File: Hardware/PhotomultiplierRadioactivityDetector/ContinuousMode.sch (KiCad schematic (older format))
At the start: 13 parts, among them U6 TL074

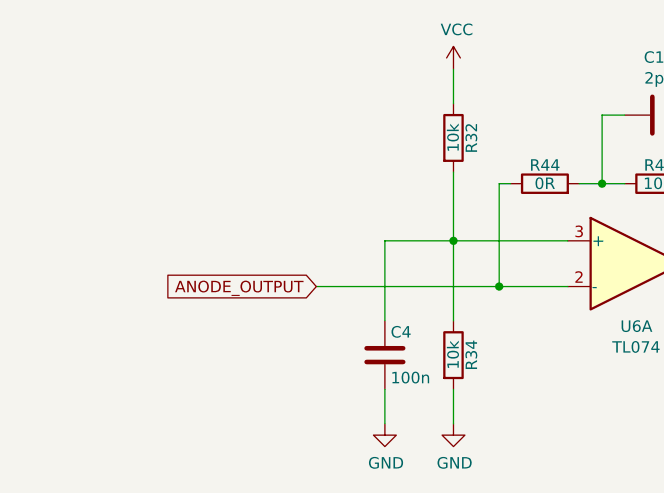
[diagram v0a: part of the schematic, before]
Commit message: add element,, footprint and 3d model for transformer
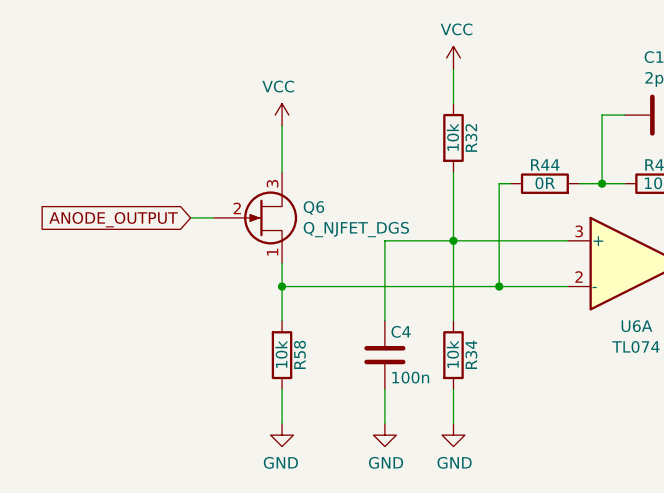
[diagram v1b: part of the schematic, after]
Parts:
- added Q6: Q_NJFET_DGS, Package_TO_SOT_SMD:SC-59, symbol Device:Q_NJFET_DGS
- added R58: 10k, Resistor_SMD:R_0805_2012Metric_Pad1.15x1.40mm_HandSolder, symbol Device:R
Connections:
- net ANODE_OUTPUT: now also Q6.2 (G); no longer R44.1, U6.2 (-)
- net GND: now also R58.1
- net VCC: now also Q6.3 (S)
- new net: Q6.1 (D), R44.1, R58.2, U6.2 (-)
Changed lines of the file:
@@
 $Descr A4 11693 8268
 encoding utf-8
-Sheet 7 7
+Sheet 6 7
 Title ""
 Date ""
@@
 	1    0    0    -1
 $EndComp
-Text GLabel 2600 3450 0    50   Input ~ 0
+Text GLabel 2050 3150 0    50   Input ~ 0
 ANODE_OUTPUT
 Wire Wire Line
 	4350 3350 4850 3350
-Wire Wire Line
-	2600 3450 3400 3450
 Text GLabel 6450 3250 2    50   Input ~ 0
 CONTONOUS_MODE_OUTPUT
+$Comp
+L power:GND #PWR?
+U 1 1 5EF7B700
+P 2450 4050
+AR Path="/5EF1F288/5EF7B700" Ref="#PWR?"  Part="1"
+AR Path="/5EDA53F3/5EF7B700" Ref="#PWR?"  Part="1"
+AR Path="/5EFA52FA/5EF7B700" Ref="#PWR?"  Part="1"
+AR Path="/5EE9D63B/5EF7B700" Ref="#PWR?"  Part="1"
+AR Path="/5EE61922/5EF7B700" Ref="#PWR069"  Part="1"
+F 0 "#PWR069" H 2450 3800 50  0001 C CNN
+F 1 "GND" H 2455 3877 50  0000 C CNN
+F 2 "" H 2450 4050 50  0001 C CNN
+F 3 "" H 2450 4050 50  0001 C CNN
+	1    2450 4050
+	-1   0    0    -1
+$EndComp
+$Comp
+L power:VCC #PWR?
+U 1 1 5EF7B706
+P 2450 2750
+AR Path="/5EFA52FA/5EF7B706" Ref="#PWR?"  Part="1"
+AR Path="/5EE9D63B/5EF7B706" Ref="#PWR?"  Part="1"
+AR Path="/5EE61922/5EF7B706" Ref="#PWR068"  Part="1"
+F 0 "#PWR068" H 2450 2600 50  0001 C CNN
+F 1 "VCC" H 2465 2923 50  0000 C CNN
+F 2 "" H 2450 2750 50  0001 C CNN
+F 3 "" H 2450 2750 50  0001 C CNN
+	1    2450 2750
+	-1   0    0    -1
+$EndComp
+$Comp
+L Device:R R?
+U 1 1 5EF7B70C
+P 2450 3750
+AR Path="/5EFA52FA/5EF7B70C" Ref="R?"  Part="1"
+AR Path="/5EE9D63B/5EF7B70C" Ref="R?"  Part="1"
+AR Path="/5EE61922/5EF7B70C" Ref="R58"  Part="1"
+F 0 "R58" V 2530 3750 50  0000 C CNN
+F 1 "10k" V 2450 3750 50  0000 C CNN
+F 2 "Resistor_SMD:R_0805_2012Metric_Pad1.15x1.40mm_HandSolder" V 2380 3750 50  0001 C CNN
+F 3 "" H 2450 3750 50  0001 C CNN
+	1    2450 3750
+	1    0    0    1
+$EndComp
+$Comp
+L Device:Q_NJFET_DGS Q?
+U 1 1 5EF7B712
+P 2350 3150
+AR Path="/5EE9D63B/5EF7B712" Ref="Q?"  Part="1"
+AR Path="/5EE61922/5EF7B712" Ref="Q6"  Part="1"
+F 0 "Q6" H 2541 3104 50  0000 L CNN
+F 1 "Q_NJFET_DGS" H 2541 3195 50  0000 L CNN
+F 2 "Package_TO_SOT_SMD:SC-59" H 2550 3250 50  0001 C CNN
+F 3 "~" H 2350 3150 50  0001 C CNN
+	1    2350 3150
+	1    0    0    1
+$EndComp
+Wire Wire Line
+	2450 3450 2450 3350
+Wire Wire Line
+	2450 3600 2450 3450
+Connection ~ 2450 3450
+Wire Wire Line
+	2450 4050 2450 3900
+Wire Wire Line
+	2450 2950 2450 2750
+Wire Wire Line
+	2050 3150 2150 3150
+Wire Wire Line
+	2450 3450 3400 3450
 $EndSCHEMATC

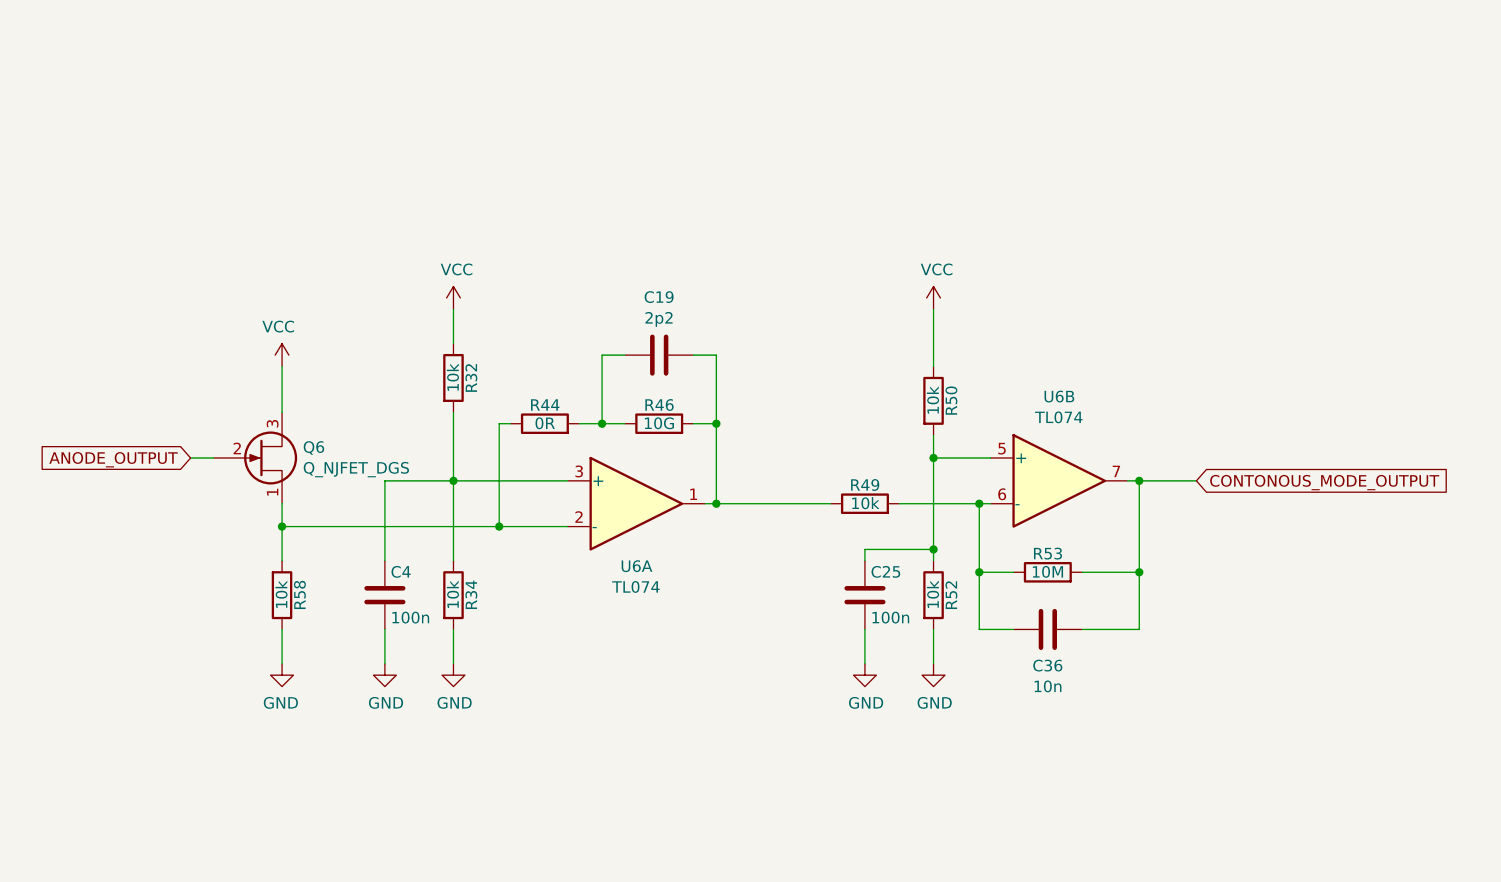
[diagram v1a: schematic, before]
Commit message: align to ltspice simulation
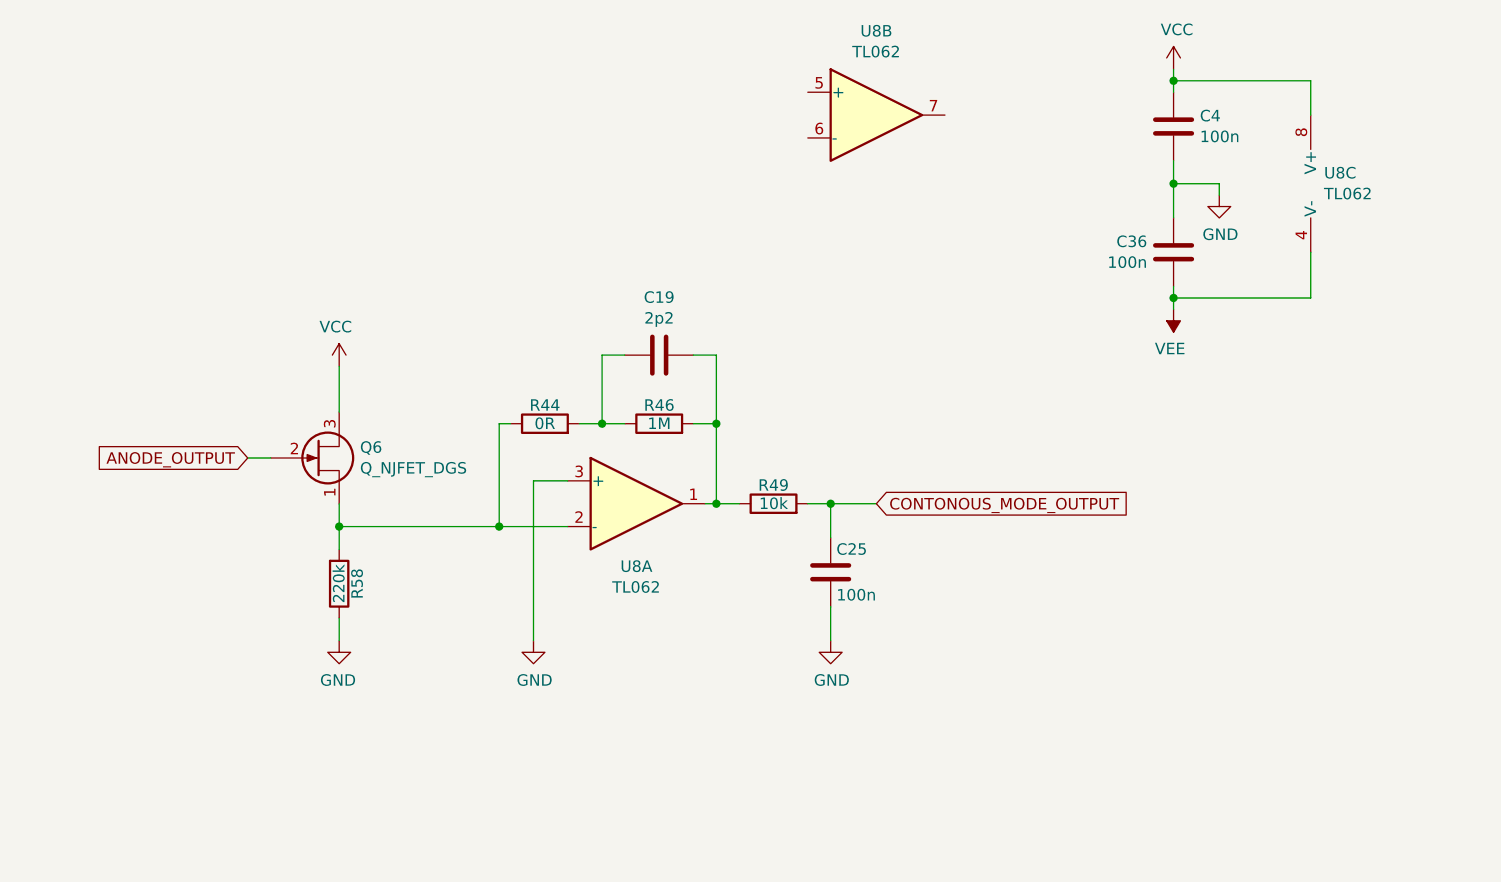
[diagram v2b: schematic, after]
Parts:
- removed R32, R34, R50, R52: 10k, Resistor_SMD:R_0805_2012Metric_Pad1.15x1.40mm_HandSolder, symbol Device:R
- removed R53: 10M, Resistor_SMD:R_0805_2012Metric_Pad1.15x1.40mm_HandSolder, symbol Device:R
- removed U6: TL074, Package_SO:SOIC-14_3.9x8.7mm_P1.27mm, symbol Amplifier_Operational:TL074
- added U8: TL062, Package_SO:SO-8_5.3x6.2mm_P1.27mm, symbol Amplifier_Operational:TL062
- C36: value 10n -> 100n
- R46: value 10G -> 1M
- R58: value 10k -> 220k
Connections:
- net CONTONOUS_MODE_OUTPUT: now also C25.1, R49.2; no longer C36.1
- net GND: now also C36.1, U8.3 (+)
- net VCC: now also C4.1, U8.8 (V+)
- net at C19.1, R46.2, R49.1: now also U8.1
- net VEE: now reaches C36.2
- net VEE: now also U8.4 (V-); no longer R49.2
- net at Q6.1 (D), R44.1, R58.2: now also U8.2 (-)
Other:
- moved on the sheet: C25, Q6, R49, R58

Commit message: simplify continous mode circuit
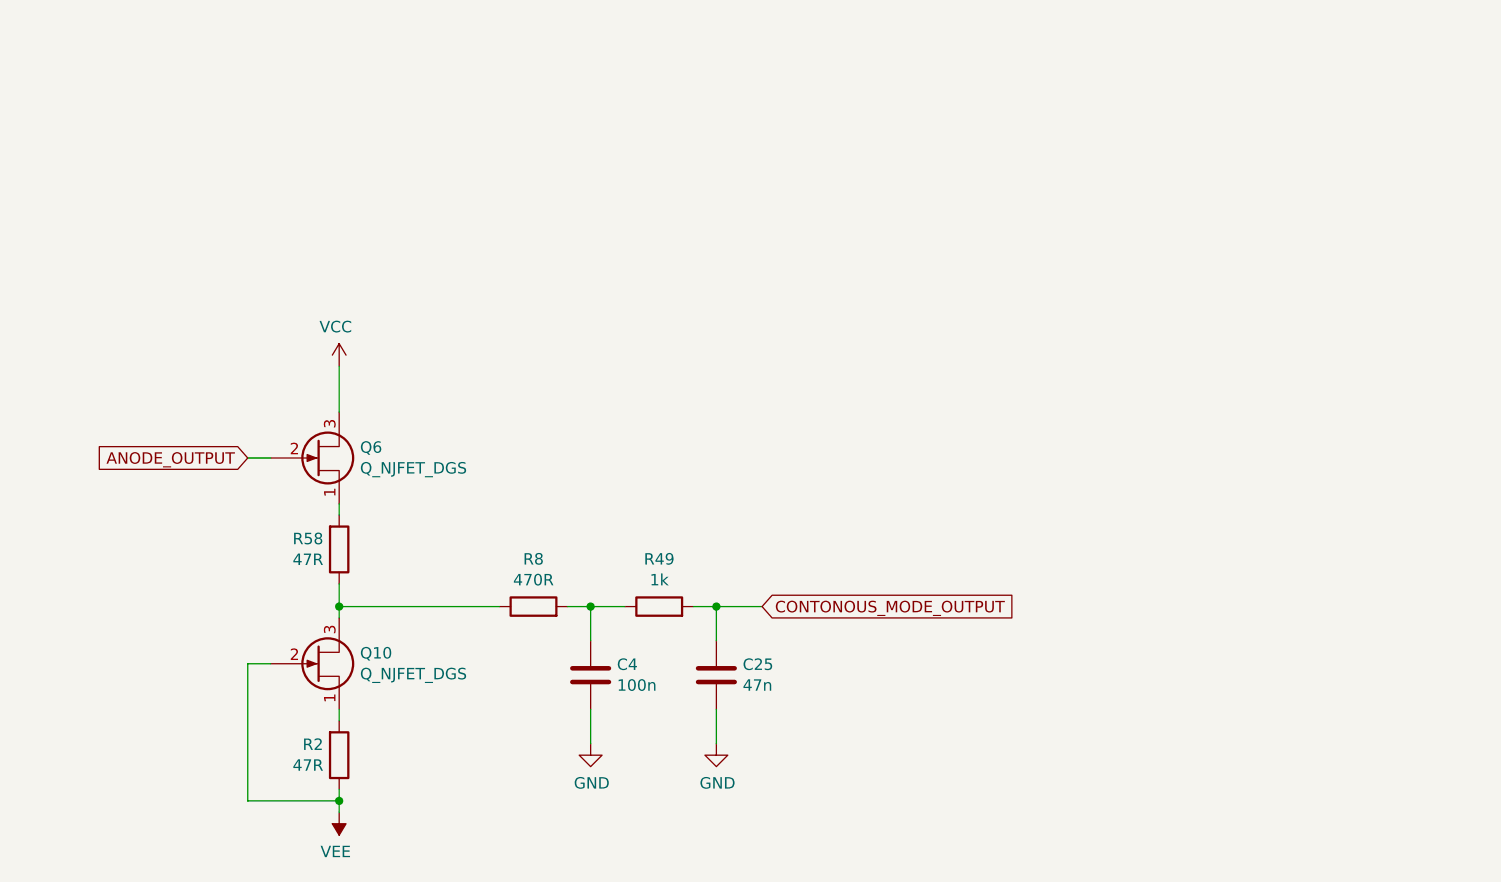
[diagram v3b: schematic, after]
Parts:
- removed C19: 2p2, Capacitor_SMD:C_0805_2012Metric_Pad1.15x1.40mm_HandSolder, symbol Device:C
- removed C36: 100n, Capacitor_SMD:C_0805_2012Metric_Pad1.15x1.40mm_HandSolder, symbol Device:C
- removed R44: 0R, Resistor_SMD:R_0805_2012Metric_Pad1.15x1.40mm_HandSolder, symbol Device:R
- removed R46: 1M, Resistor_SMD:R_0805_2012Metric_Pad1.15x1.40mm_HandSolder, symbol Device:R
- removed U8: TL062, Package_SO:SO-8_5.3x6.2mm_P1.27mm, symbol Amplifier_Operational:TL062
- added Q10: Q_NJFET_DGS, Package_TO_SOT_SMD:SC-59, symbol Device:Q_NJFET_DGS
- added R2: 47R, Resistor_SMD:R_0805_2012Metric_Pad1.15x1.40mm_HandSolder, symbol Device:R
- added R8: 470R, Resistor_SMD:R_0805_2012Metric_Pad1.15x1.40mm_HandSolder, symbol Device:R
- C25: value 100n -> 47n
- R49: value 10k -> 1k
- R58: value 220k -> 47R
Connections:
- net GND: no longer R58.1
- net VCC: no longer C4.1
- net VEE: now also Q10.2 (G), R2.1
- net at R49.1: now also C4.1, R8.2
- new net: Q10.3 (S), R58.1, R8.1
- new net: Q10.1 (D), R2.2
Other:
- moved on the sheet: C25, R49, R58
